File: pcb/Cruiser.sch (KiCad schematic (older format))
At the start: 37 parts, among them J1 USB-A, P1 BDM, SW1 Load/Run, SW2 Reset, U1 FT232RL, U2 MC9S12XDP512, X1 16MHz

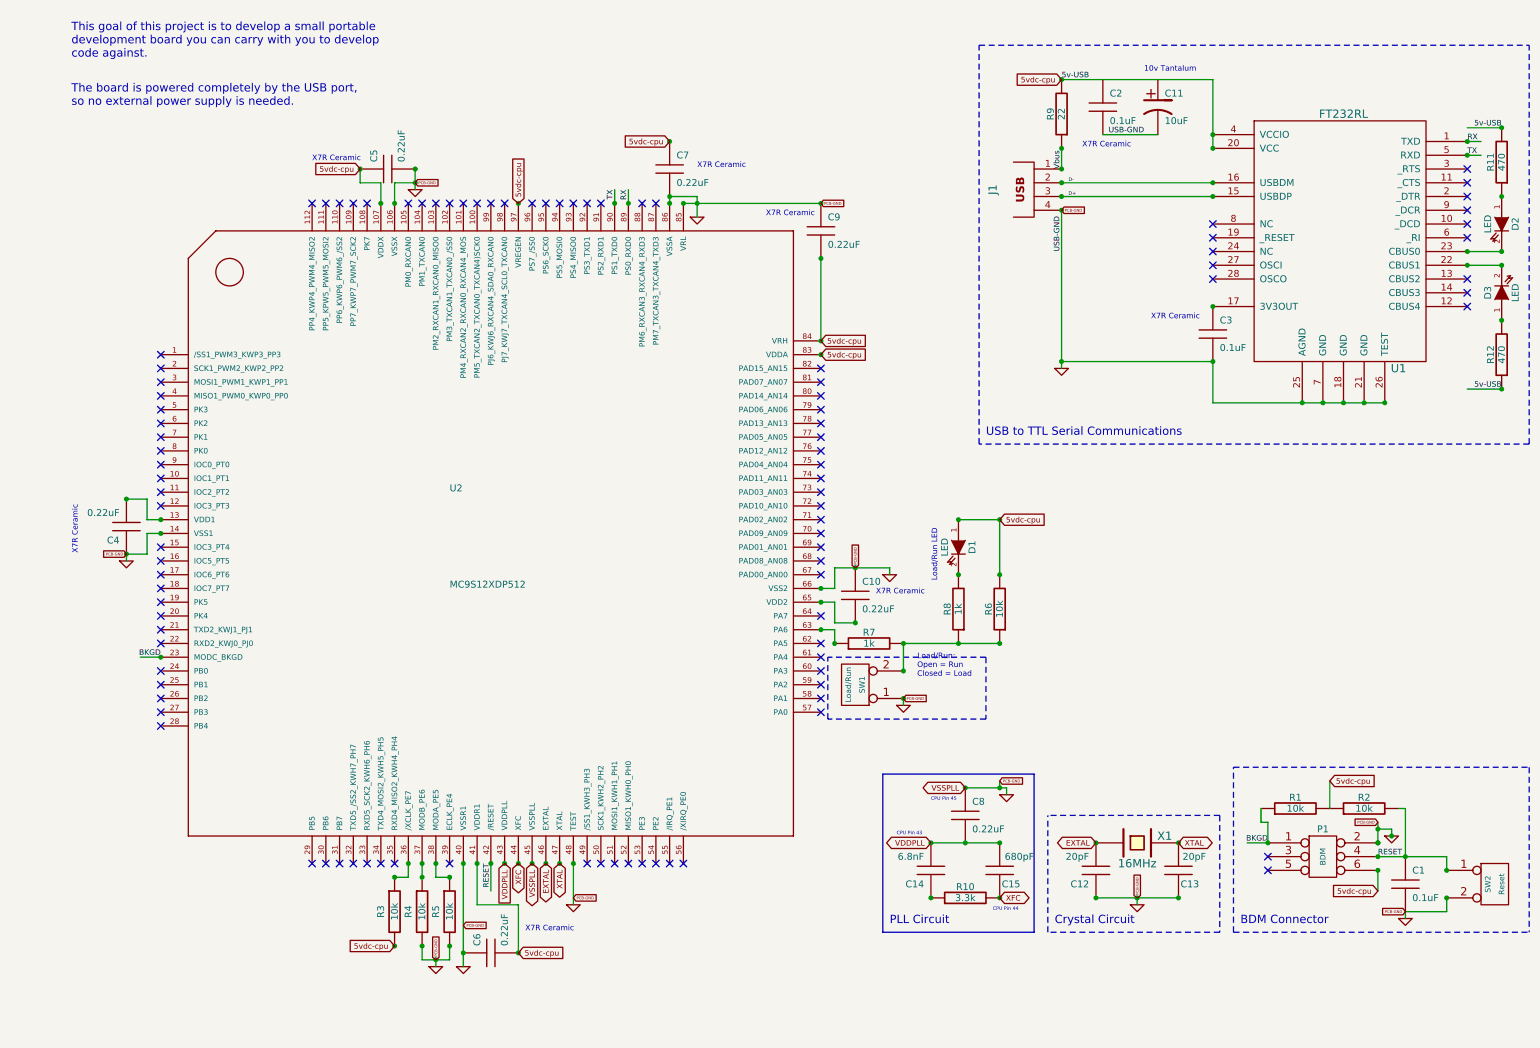
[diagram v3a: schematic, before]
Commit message: Deleted non-essential capacitors and created a new PCB layout that is less than 50mm x 50mm (1.969" x 1.969") which looks like a key.
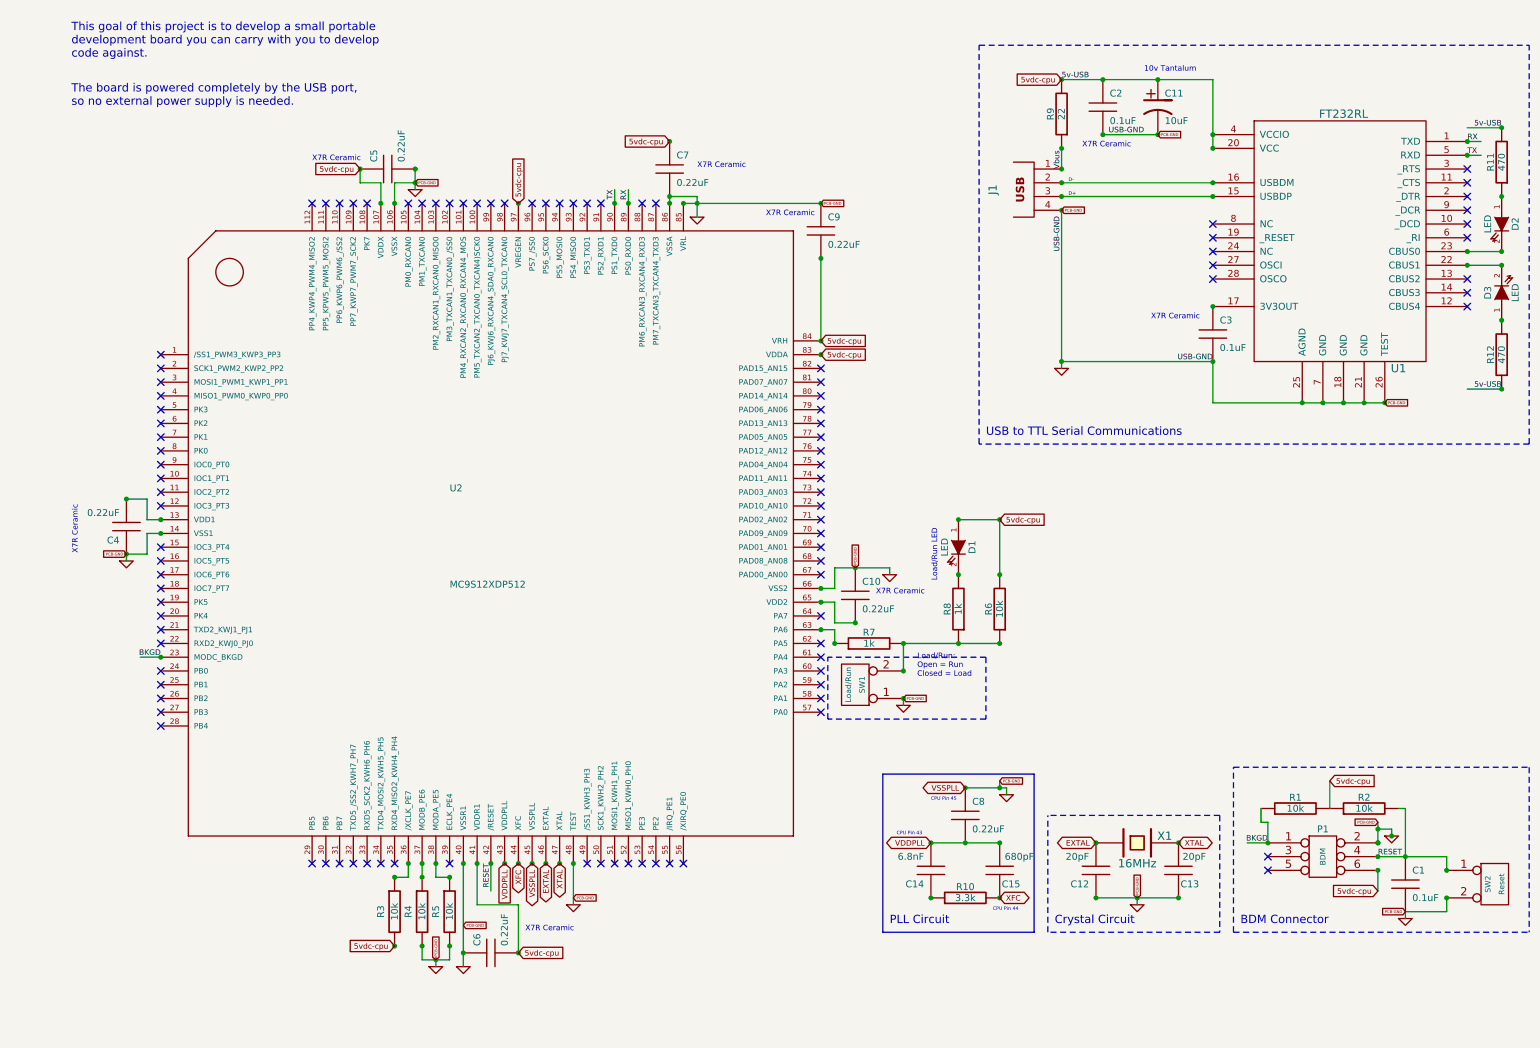
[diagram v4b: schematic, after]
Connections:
- wire segments 88 -> 106
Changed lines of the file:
@@
-EESchema Schematic File Version 2  date Sun 04 Nov 2012 10:56:37 AM EST
+EESchema Schematic File Version 2  date Sun 04 Nov 2012 12:03:22 PM EST
 LIBS:opto
 LIBS:Jaguar
@@
 Comment4 ""
 $EndDescr
+Text GLabel 10100 3150 2    20   Input ~ 0
+PCB-GND
+Connection ~ 8050 1200
+Connection ~ 8450 1200
+Connection ~ 8450 800
+Connection ~ 8050 800
+Text GLabel 8450 1200 2    20   Input ~ 0
+PCB-GND
+Text Label 8850 2850 2    40   ~ 0
+USB-GND
 Wire Notes Line
 	9000 7000 11150 7000
 Wire Wire Line
-	7750 2900 7750 1750
+	7750 2900 7750 2850
+Wire Wire Line
+	7750 2850 7750 1750
 Wire Wire Line
 	10950 1150 10700 1150
@@
 	8900 6150 8900 7000
 Wire Wire Line
-	8000 6750 8600 6750
+	8000 6750 8300 6750
+Wire Wire Line
+	8300 6750 8600 6750
 Connection ~ 2900 7100
 Connection ~ 2900 6600
@@
 	3300 7100 3300 7200
 Wire Wire Line
-	3300 7200 3100 7200
+	3300 7200 3200 7200
+Wire Wire Line
+	3200 7200 3100 7200
 Wire Wire Line
 	3100 7200 3100 7100
@@
 	10550 6550 10550 6450
 Wire Wire Line
-	10550 6450 10050 6450
+	10550 6450 10250 6450
+Wire Wire Line
+	10250 6450 10050 6450
 Connection ~ 6000 2100
 Connection ~ 6000 1700
@@
 	6100 4500 6100 4350
 Wire Wire Line
-	6100 4350 6500 4350
+	6100 4350 6250 4350
+Wire Wire Line
+	6250 4350 6500 4350
 Wire Wire Line
 	950  3850 1100 3850
@@
 	7350 6000 7350 5950
 Wire Wire Line
-	7350 5950 7050 5950
+	7350 5950 7300 5950
+Wire Wire Line
+	7300 5950 7050 5950
 Connection ~ 3050 1550
 Wire Wire Line
@@
 Connection ~ 10050 6350
 Wire Wire Line
-	6800 6350 7300 6350
+	6800 6350 7050 6350
+Wire Wire Line
+	7050 6350 7300 6350
 Wire Wire Line
 	1100 3850 1100 4000
@@
 Connection ~ 7300 5950
 Wire Wire Line
-	5100 1650 5100 1800
-Wire Wire Line
-	6000 1700 5000 1700
+	5100 1650 5100 1700
+Wire Wire Line
+	5100 1700 5100 1800
+Wire Wire Line
+	6000 1700 5100 1700
+Wire Wire Line
+	5100 1700 5000 1700
 Wire Wire Line
 	2900 1550 3050 1550
@@
 Connection ~ 4900 1250
 Wire Wire Line
-	10050 6350 10050 6200
+	10050 6350 10050 6250
+Wire Wire Line
+	10050 6250 10050 6200
 Connection ~ 10050 6250
 Wire Wire Line
-	3050 1600 3050 1450
+	3050 1600 3050 1550
+Wire Wire Line
+	3050 1550 3050 1450
 Wire Wire Line
 	3100 6500 3100 6600
@@
 Connection ~ 3200 7200
 Wire Wire Line
-	3400 6500 3400 7250
+	3400 6500 3400 7150
+Wire Wire Line
+	3400 7150 3400 7250
 Connection ~ 3400 7150
 Connection ~ 3800 7150
@@
 	9000 7000 9000 5800
 Wire Wire Line
-	6600 4900 7300 4900
+	6600 4900 7000 4900
+Wire Wire Line
+	7000 4900 7300 4900
 Connection ~ 7000 4900
 Connection ~ 7750 2850
@@
 Connection ~ 10700 1250
 Wire Wire Line
-	8850 3150 10100 3150
+	8850 3150 9500 3150
+Wire Wire Line
+	9500 3150 9650 3150
+Wire Wire Line
+	9650 3150 9800 3150
+Wire Wire Line
+	9800 3150 9950 3150
+Wire Wire Line
+	9950 3150 10100 3150
 Connection ~ 7750 800
 Connection ~ 7750 1300
@@
 	7750 800  8850 800
 Wire Wire Line
-	8850 800  8850 1300
+	8850 800  8850 1200
+Wire Wire Line
+	8850 1200 8850 1300
 Connection ~ 10950 2050
 Connection ~ 10950 1650

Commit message: Updated git hash to 9b4c4c8ada on the schematic and the PCB.
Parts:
- added H1: Hole, symbol CONN_1
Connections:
- wire segments 106 -> 88
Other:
- note added: "Keychain Hole"
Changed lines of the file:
@@
-EESchema Schematic File Version 2  date Sun 04 Nov 2012 12:03:22 PM EST
+EESchema Schematic File Version 2  date Sun 04 Nov 2012 02:43:39 PM EST
 LIBS:opto
 LIBS:Jaguar
@@
 $Descr A4 11700 8267
 Sheet 1 1
-Title "Cruiser"
+Title "Cruiser Dev Board"
 Date "4 nov 2012"
 Rev "0.1-alpha"
-Comp "git hash: 957894db06"
-Comment1 ""
+Comp "Andy Goss"
+Comment1 "git hash: 9b4c4c8ada"
 Comment2 ""
 Comment3 ""
 Comment4 ""
 $EndDescr
+Text GLabel 9850 4700 0    20   Input ~ 0
+PCB-GND
+Text Notes 9600 4850 0    60   ~ 0
+Keychain Hole
+$Comp
+L CONN_1 H1
+U 1 1 5096BAD1
+P 10000 4700
+F 0 "H1" H 10080 4700 40  0000 L CNN
+F 1 "Hole" H 10000 4755 30  0001 C CNN
+	1    10000 4700
+	1    0    0    -1
+$EndComp
 Text GLabel 10100 3150 2    20   Input ~ 0
 PCB-GND
@@
 	9000 7000 11150 7000
 Wire Wire Line
-	7750 2900 7750 2850
-Wire Wire Line
-	7750 2850 7750 1750
+	7750 2900 7750 1750
 Wire Wire Line
 	10950 1150 10700 1150
@@
 	8900 6150 8900 7000
 Wire Wire Line
-	8000 6750 8300 6750
-Wire Wire Line
-	8300 6750 8600 6750
+	8000 6750 8600 6750
 Connection ~ 2900 7100
 Connection ~ 2900 6600
@@
 	3300 7100 3300 7200
 Wire Wire Line
-	3300 7200 3200 7200
-Wire Wire Line
-	3200 7200 3100 7200
+	3300 7200 3100 7200
 Wire Wire Line
 	3100 7200 3100 7100
@@
 	10550 6550 10550 6450
 Wire Wire Line
-	10550 6450 10250 6450
-Wire Wire Line
-	10250 6450 10050 6450
+	10550 6450 10050 6450
 Connection ~ 6000 2100
 Connection ~ 6000 1700
@@
 	6100 4500 6100 4350
 Wire Wire Line
-	6100 4350 6250 4350
-Wire Wire Line
-	6250 4350 6500 4350
+	6100 4350 6500 4350
 Wire Wire Line
 	950  3850 1100 3850
@@
 	7350 6000 7350 5950
 Wire Wire Line
-	7350 5950 7300 5950
-Wire Wire Line
-	7300 5950 7050 5950
+	7350 5950 7050 5950
 Connection ~ 3050 1550
 Wire Wire Line
@@
 Connection ~ 10050 6350
 Wire Wire Line
-	6800 6350 7050 6350
-Wire Wire Line
-	7050 6350 7300 6350
+	6800 6350 7300 6350
 Wire Wire Line
 	1100 3850 1100 4000
@@
 Connection ~ 7300 5950
 Wire Wire Line
-	5100 1650 5100 1700
-Wire Wire Line
-	5100 1700 5100 1800
-Wire Wire Line
-	6000 1700 5100 1700
-Wire Wire Line
-	5100 1700 5000 1700
+	5100 1650 5100 1800
+Wire Wire Line
+	6000 1700 5000 1700
 Wire Wire Line
 	2900 1550 3050 1550
@@
 Connection ~ 4900 1250
 Wire Wire Line
-	10050 6350 10050 6250
-Wire Wire Line
-	10050 6250 10050 6200
+	10050 6350 10050 6200
 Connection ~ 10050 6250
 Wire Wire Line
-	3050 1600 3050 1550
-Wire Wire Line
-	3050 1550 3050 1450
+	3050 1600 3050 1450
 Wire Wire Line
 	3100 6500 3100 6600
@@
 Connection ~ 3200 7200
 Wire Wire Line
-	3400 6500 3400 7150
-Wire Wire Line
-	3400 7150 3400 7250
+	3400 6500 3400 7250
 Connection ~ 3400 7150
 Connection ~ 3800 7150
@@
 	9000 7000 9000 5800
 Wire Wire Line
-	6600 4900 7000 4900
-Wire Wire Line
-	7000 4900 7300 4900
+	6600 4900 7300 4900
 Connection ~ 7000 4900
 Connection ~ 7750 2850
@@
 Connection ~ 10700 1250
 Wire Wire Line
-	8850 3150 9500 3150
-Wire Wire Line
-	9500 3150 9650 3150
-Wire Wire Line
-	9650 3150 9800 3150
-Wire Wire Line
-	9800 3150 9950 3150
-Wire Wire Line
-	9950 3150 10100 3150
+	8850 3150 10100 3150
 Connection ~ 7750 800
 Connection ~ 7750 1300
@@
 	7750 800  8850 800
 Wire Wire Line
-	8850 800  8850 1200
-Wire Wire Line
-	8850 1200 8850 1300
+	8850 800  8850 1300
 Connection ~ 10950 2050
 Connection ~ 10950 1650

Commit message: Initial commit of the Cruiser-BOM.ods file.
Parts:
- SW1: value Load/Run -> Load
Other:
- note added: "Load SW1:\nOpen = Run\nClosed = Load"
- note removed: "Load/Run:\nOpen = Run\nClosed = Load"
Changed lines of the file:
@@
-EESchema Schematic File Version 2  date Sun 04 Nov 2012 02:43:39 PM EST
+EESchema Schematic File Version 2  date Sun 04 Nov 2012 03:02:35 PM EST
 LIBS:opto
 LIBS:Jaguar
@@
 P 6250 5200
 F 0 "SW1" V 6200 5200 40  0000 C CNN
-F 1 "Load/Run" V 6300 5200 40  0000 C CNN
+F 1 "Load" V 6300 5200 40  0000 C CNN
 	1    6250 5200
 	-1   0    0    1
@@
 Text Notes 6400 4550 0    40   ~ 0
 X7R Ceramic
-Text Notes 6700 5150 0    40   ~ 0
-Load/Run:\nOpen = Run\nClosed = Load
+Text Notes 6700 5100 0    40   ~ 0
+Load SW1:\nOpen = Run\nClosed = Load
 $Comp
 L C C4
